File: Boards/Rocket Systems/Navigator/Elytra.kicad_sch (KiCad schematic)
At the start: 3 parts, among them U9 SQJA36EP-T1_GE3

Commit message: HYDRA Update
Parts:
- removed R26: R, symbol Device:R
- removed U9: SQJA36EP-T1_GE3, PowerPAK_SO-8L_3_VIS, symbol SQJA36EP-T1-GE3:SQJA36EP-T1_GE3
- added IC4: LMV321LILT, SOT95P280X145-5N, symbol LMV321LILT:LMV321LILT
- added R26: 24K, RES_0402, symbol Device:R
- added R26, R36, R39: 100K, RES_0603, symbol Device:R
- added R27: 2.7K, RES_0402, symbol Device:R
- added R28: 750, RES_0805, symbol Device:R
- added R28: 1.3K, RES_0402, symbol Device:R
- added R29: 22K, RES_0402, symbol Device:R
- added R30, R40: 10k, RES_0402, symbol Device:R
- added R31: 50, RES_0603, symbol Device:R
- added R32: 6.2K, RES_0603, symbol Device:R
- added R33: 200K, RES_0603, symbol Device:R
- added R34: 500, RES_0603, symbol Device:R
- added R35: 12K, RES_0603, symbol Device:R
- added R37: 1K, RES_0603, symbol Device:R
- added R38: 24K, RES_0603, symbol Device:R
- added U10, U11, U9: NCR321UX, TSOP6_SOT457_NEX, symbol NCR321UX:NCR321UX
- R8: value R -> 10k; footprint (none) -> RES_0402
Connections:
- net GND: now also IC4.2 (V-), R26.2, R30.2, R40.2, U10.4 (GND), U11.4 (GND), U9.4 (GND)
- net PYRO1: now reaches R8.1
- net PYRO1: now also U9.1 (VEN)
- new net: IC4.3 (-), R26.2, R28.2, R32.2, R33.2, R35.2, R36.2, R38.2, R39.2
- new net: R37.2, R38.1
- new net: U10.2 (IOUT), U10.3 (IOUT), U10.5 (IOUT)
- new net: R34.2, R35.1
- new net: R26.1, R27.1
- new net: IC4.1 (+), R27.2, R28.1
- new net: IC4.4, R28.1
- new net: R28.2, R29.1
- new net: R31.2, R32.1
- new net: U9.2 (IOUT), U9.3 (IOUT), U9.5 (IOUT)
- new net: U11.2 (IOUT), U11.3 (IOUT), U11.5 (IOUT)
- new net +3.3V: IC4.5 (V+)
- new net +5V: R29.2
- new net PYRO2: R30.1, U10.1 (VEN)
- new net PYRO3: R40.1, U11.1 (VEN)
- new net V1: R31.1
- new net V2: R33.1
- new net V3: R34.1
- new net V4: R36.1
- new net V5: R37.1
- new net V6: R26.1, R39.1
- no-connect marks 0 -> 3

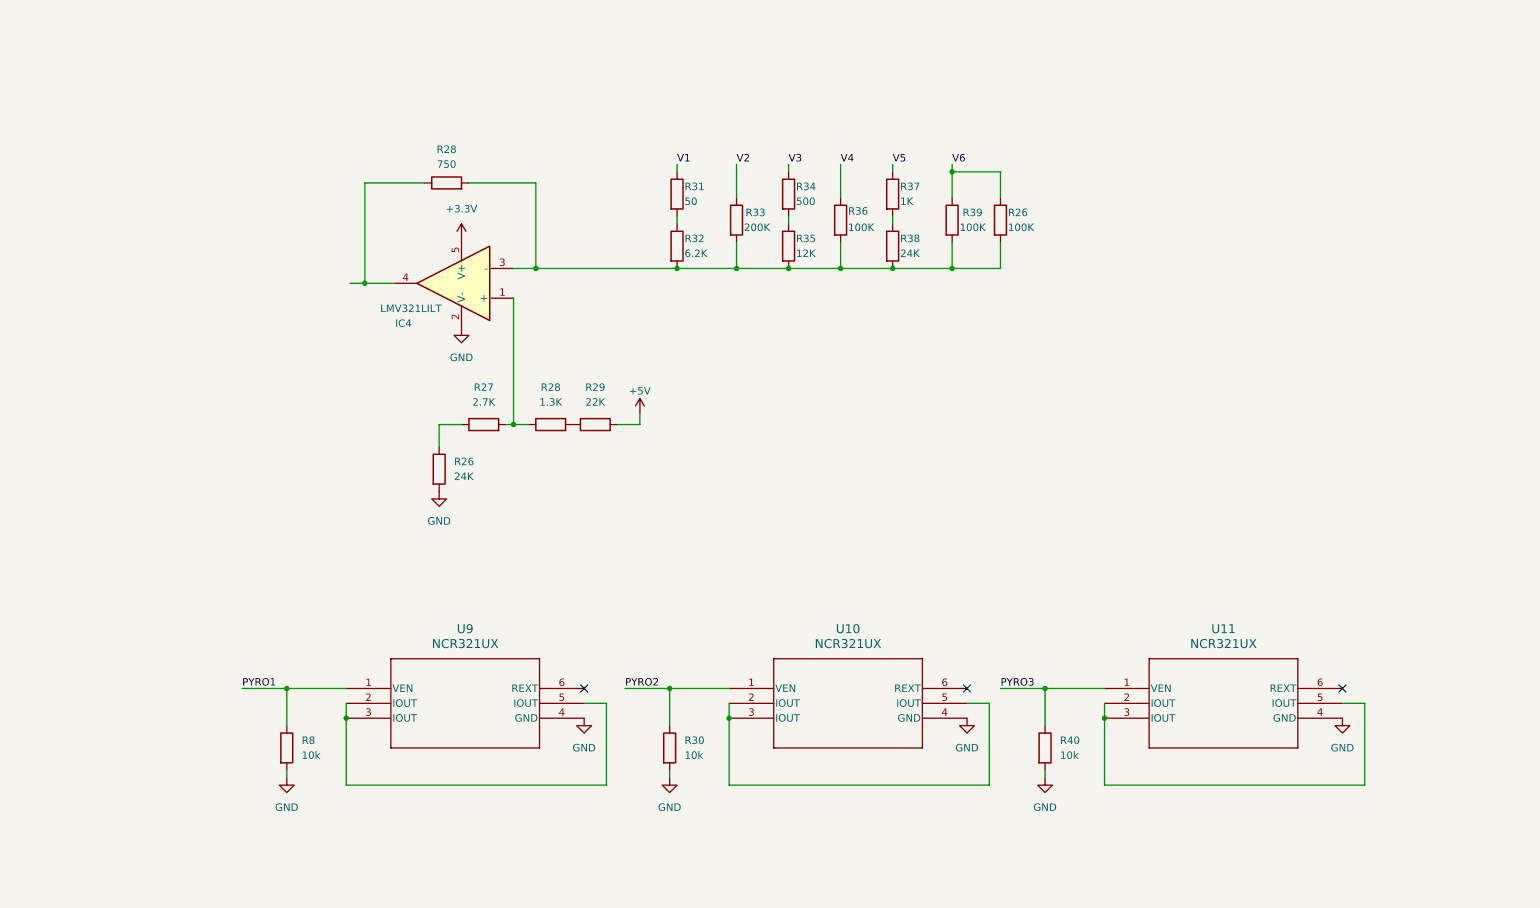
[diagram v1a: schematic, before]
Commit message: elytra added to navigator
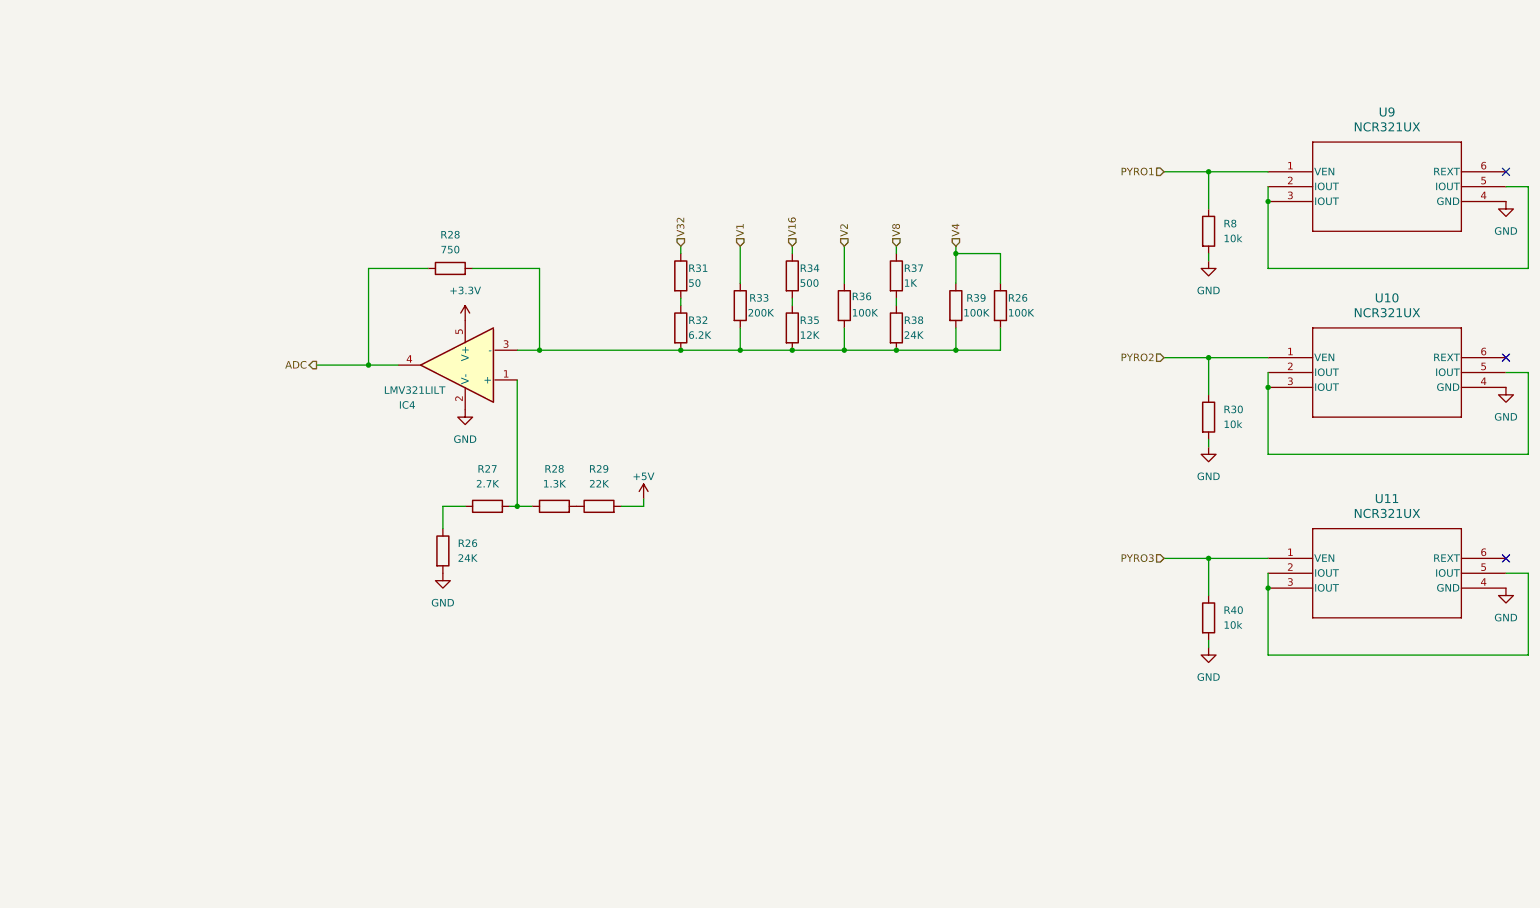
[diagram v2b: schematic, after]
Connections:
- net V6 is gone; now on net V4: R26.1, R39.1
- net V1: now also R33.1; no longer R31.1
- net V2: now also R36.1; no longer R33.1
- net V4: no longer R36.1
- net ADC: now reaches IC4.4, R28.1
- net V3 renamed V16
- net V5 renamed V8
- new net V32: R31.1
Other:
- moved on the sheet: IC4, R26, R27, R28, R29, R30, R31, R32, R33, R34, R35, R36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

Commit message: drc and new components added
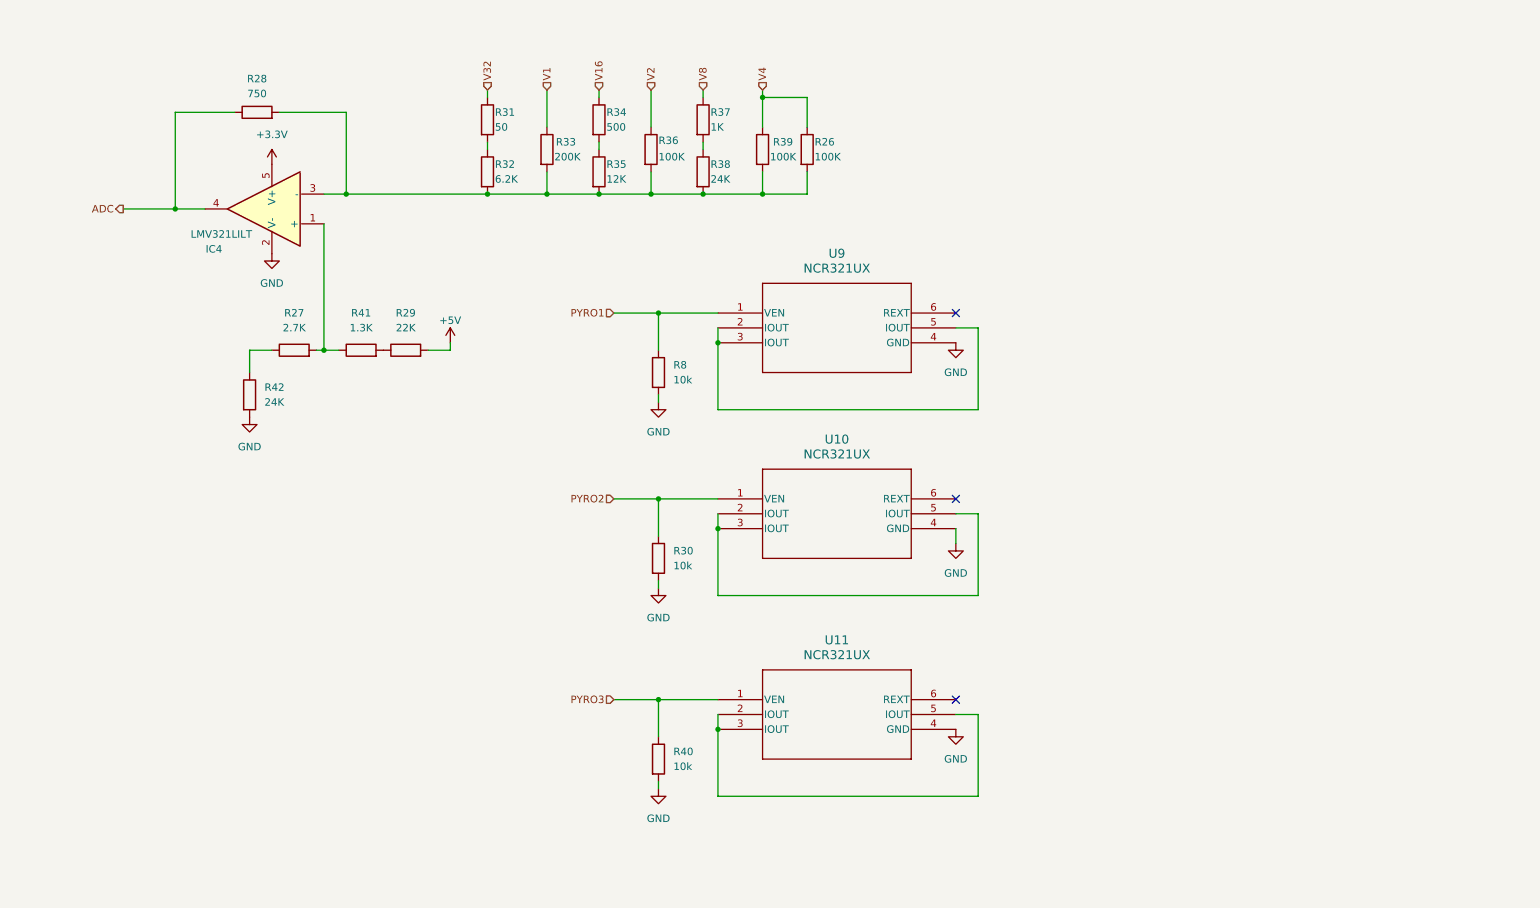
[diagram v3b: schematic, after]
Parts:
- removed R26: 24K, RES_0402, symbol Device:R
- removed R28: 1.3K, RES_0402, symbol Device:R
- added R41: 1.3K, RES_0402, symbol Device:R
- added R42: 24K, RES_0402, symbol Device:R
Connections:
- net GND: now also R42.2
- net at R27.1: now also R42.1
- net at IC4.1 (+), R27.2: now also R41.1
- net at R29.1: now also R41.2
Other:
- moved on the sheet: IC4, R26, R27, R28, R29, R30, R31, R32, R33, R34, R35, R36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

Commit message: Nav Update
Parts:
- IC4: footprint SOT95P280X145-5N -> LMV321LILT:SOT95P280X145-5N
- R26, R31, R32, R33, R34, R35, R36, R37, R38, R39: footprint RES_0603 -> Resistor-0603:RES_0603
- R27, R29, R30, R40, R41, R42, R8: footprint RES_0402 -> Resistor-0402:RES_0402
- R28: footprint RES_0805 -> Resistor-0805:RES_0805
- U10, U11, U9: footprint TSOP6_SOT457_NEX -> LED Driver_NCR321UX:TSOP6_SOT457_NEX
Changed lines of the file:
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@@
 			)
 		)
-		(property "Footprint" "RES_0603"
+		(property "Footprint" "Resistor-0603:RES_0603"
 			(at 111.252 34.29 90)
 			(effects
@@
 			)
 		)
-		(property "Footprint" "RES_0603"
+		(property "Footprint" "Resistor-0603:RES_0603"
 			(at 130.302 34.29 90)
 			(effects
@@
 			)
 		)
-		(property "Footprint" "RES_0603"
+		(property "Footprint" "Resistor-0603:RES_0603"
 			(at 120.142 29.21 90)
 			(effects
@@
 			)
 		)
-		(property "Footprint" "TSOP6_SOT457_NEX"
+		(property "Footprint" "LED Driver_NCR321UX:TSOP6_SOT457_NEX"
 			(at 124.46 93.98 0)
 			(effects
@@
 			)
 		)
-		(property "Footprint" "RES_0402"
+		(property "Footprint" "Resistor-0402:RES_0402"
 			(at 42.672 76.2 90)
 			(effects
@@
 			)
 		)
-		(property "Footprint" "RES_0603"
+		(property "Footprint" "Resistor-0603:RES_0603"
 			(at 102.362 38.1 90)
 			(effects
@@
 			)
 		)
-		(property "Footprint" "RES_0402"
+		(property "Footprint" "Resistor-0402:RES_0402"
 			(at 52.07 70.358 90)
 			(effects
@@
 			)
 		)
-		(property "Footprint" "RES_0805"
+		(property "Footprint" "Resistor-0805:RES_0805"
 			(at 45.72 29.718 90)
 			(effects
@@
 			)
 		)
-		(property "Footprint" "SOT95P280X145-5N"
+		(property "Footprint" "LMV321LILT:SOT95P280X145-5N"
 			(at 31.75 136.83 0)
 			(effects
@@
 			)
 		)
-		(property "Footprint" "RES_0603"
+		(property "Footprint" "Resistor-0603:RES_0603"
 			(at 120.142 38.1 90)
 			(effects
@@
 			)
 		)
-		(property "Footprint" "RES_0603"
+		(property "Footprint" "Resistor-0603:RES_0603"
 			(at 102.362 29.21 90)
 			(effects
@@
 			)
 		)
-		(property "Footprint" "RES_0402"
+		(property "Footprint" "Resistor-0402:RES_0402"
 			(at 112.522 104.14 90)
 			(effects
@@
 			)
 		)
-		(property "Footprint" "RES_0603"
+		(property "Footprint" "Resistor-0603:RES_0603"
 			(at 93.472 34.29 90)
 			(effects
@@
 			)
 		)
-		(property "Footprint" "RES_0603"
+		(property "Footprint" "Resistor-0603:RES_0603"
 			(at 83.312 38.1 90)
 			(effects
@@
 			)
 		)
-		(property "Footprint" "RES_0603"
+		(property "Footprint" "Resistor-0603:RES_0603"
 			(at 137.922 34.29 90)
 			(effects
@@
 			)
 		)
-		(property "Footprint" "TSOP6_SOT457_NEX"
+		(property "Footprint" "LED Driver_NCR321UX:TSOP6_SOT457_NEX"
 			(at 124.46 62.23 0)
 			(effects
@@
 			)
 		)
-		(property "Footprint" "RES_0402"
+		(property "Footprint" "Resistor-0402:RES_0402"
 			(at 63.5 70.358 90)
 			(effects
@@
 			)
 		)
-		(property "Footprint" "RES_0402"
+		(property "Footprint" "Resistor-0402:RES_0402"
 			(at 112.522 138.43 90)
 			(effects
@@
 			)
 		)
-		(property "Footprint" "RES_0402"
+		(property "Footprint" "Resistor-0402:RES_0402"
 			(at 71.12 70.358 90)
 			(effects
@@
 			)
 		)
-		(property "Footprint" "RES_0603"
+		(property "Footprint" "Resistor-0603:RES_0603"
 			(at 83.312 29.21 90)
 			(effects
@@
 			)
 		)
-		(property "Footprint" "RES_0402"
+		(property "Footprint" "Resistor-0402:RES_0402"
 			(at 112.522 72.39 90)
 			(effects
@@
 			)
 		)
-		(property "Footprint" "TSOP6_SOT457_NEX"
+		(property "Footprint" "LED Driver_NCR321UX:TSOP6_SOT457_NEX"
 			(at 124.46 128.27 0)
 			(effects

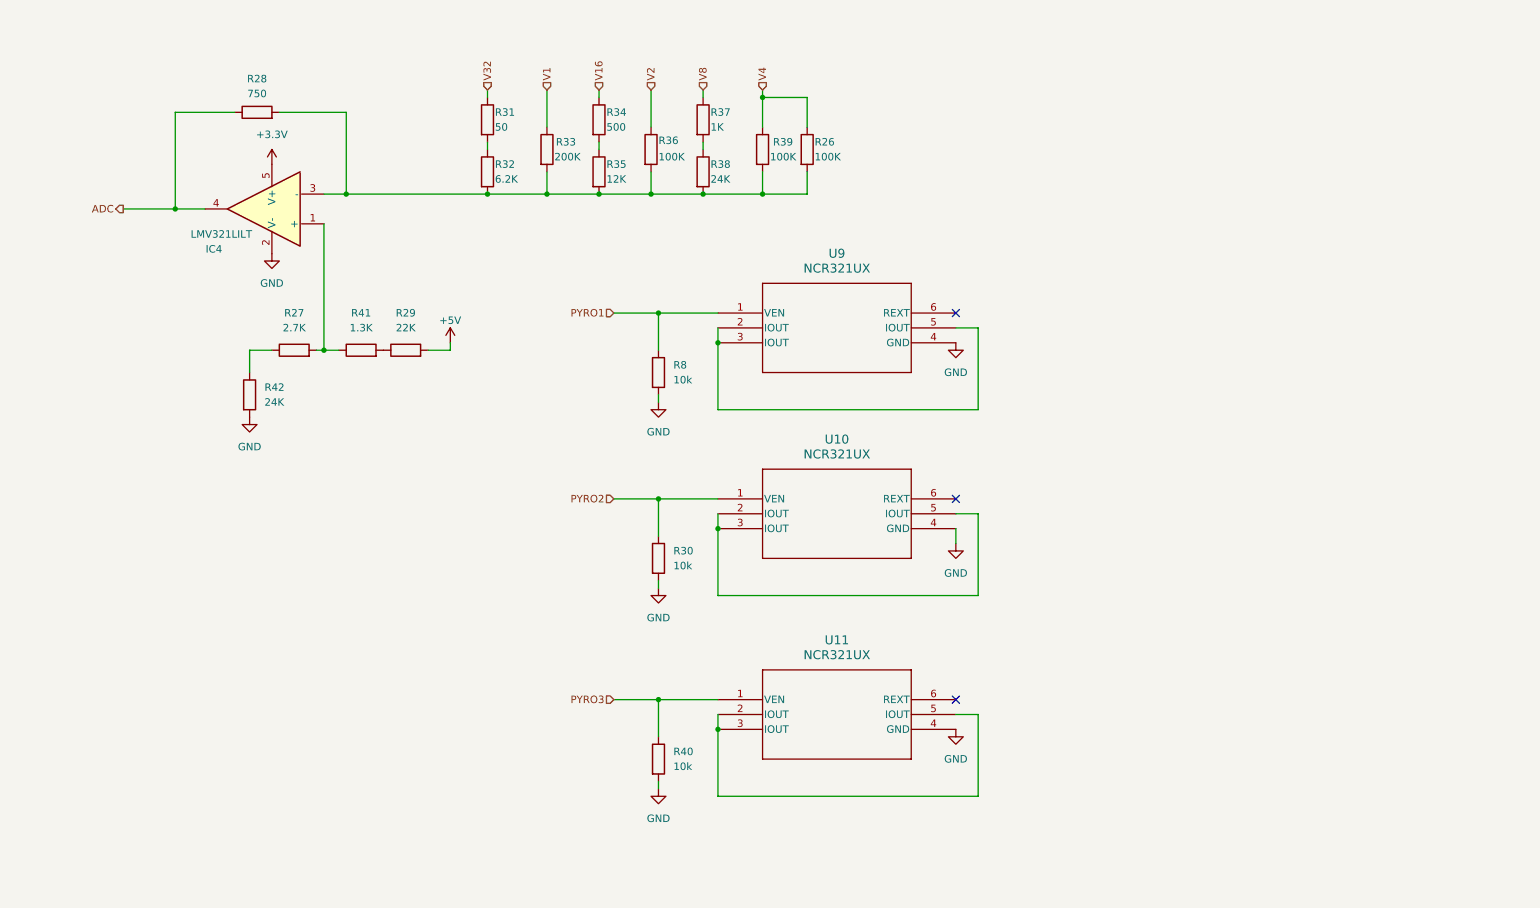
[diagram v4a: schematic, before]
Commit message: elytra added and full routing done
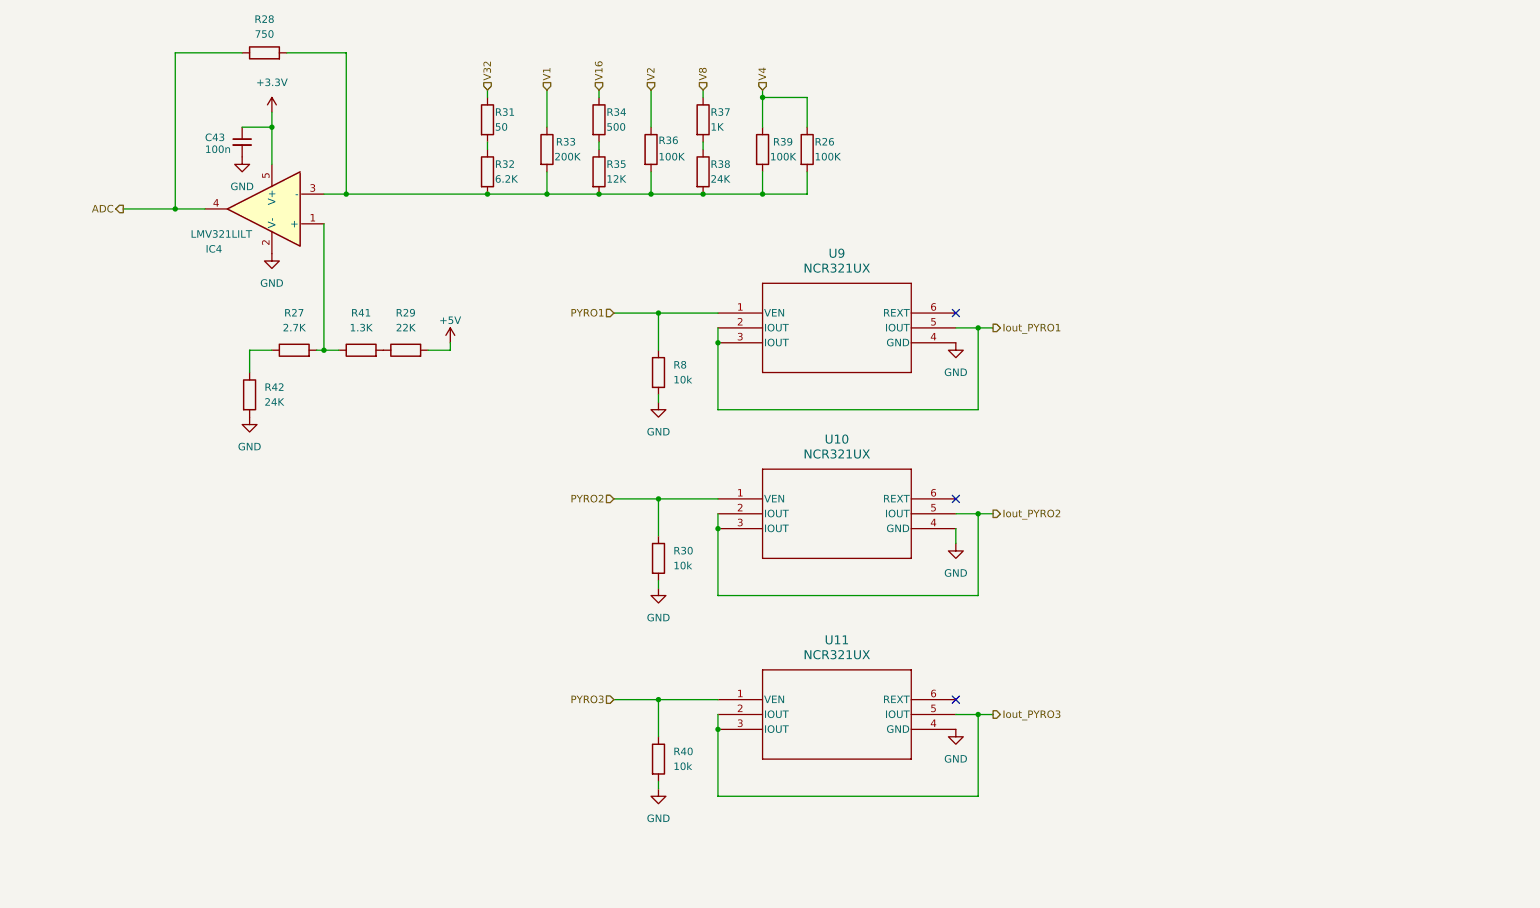
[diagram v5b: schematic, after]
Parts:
- added C43: 100n, Capacitor-0402:Capacitor_0402, symbol Device:C_Small
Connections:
- net +3.3V: now also C43.1
- net GND: now also C43.2
- net Iout_PYRO2: now reaches U10.2 (IOUT), U10.3 (IOUT), U10.5 (IOUT)
- net Iout_PYRO1: now reaches U9.2 (IOUT), U9.3 (IOUT), U9.5 (IOUT)
- net Iout_PYRO3: now reaches U11.2 (IOUT), U11.3 (IOUT), U11.5 (IOUT)
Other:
- moved on the sheet: R28

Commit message: Navigator Final Update - DFM corrections
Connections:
- net Iout_PYRO1 is gone; now on net PYRO1: U9.2 (IOUT), U9.3 (IOUT), U9.5 (IOUT)
- net Iout_PYRO2 is gone; now on net PYRO2: U10.2 (IOUT), U10.3 (IOUT), U10.5 (IOUT)
- net Iout_PYRO3 is gone; now on net PYRO3: U11.2 (IOUT), U11.3 (IOUT), U11.5 (IOUT)
- net PYRO1: no longer R8.1, U9.1 (VEN)
- net PYRO2: no longer R30.1, U10.1 (VEN)
- net PYRO3: no longer R40.1, U11.1 (VEN)
- new net RECOVERY1: R8.1, U9.1 (VEN)
- new net RECOVERY2: R30.1, U10.1 (VEN)
- new net RECOVERY3: R40.1, U11.1 (VEN)
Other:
- moved on the sheet: C43, IC4, R26, R27, R28, R29, R30, R31, R32, R33, R34, R35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
